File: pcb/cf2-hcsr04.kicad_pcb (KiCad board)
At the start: 2 copper layers, 25.2 x 27.3 mm, 3 parts, among them P1 CF_EXP_LEFT, P2 CF_EXP_RIGHT

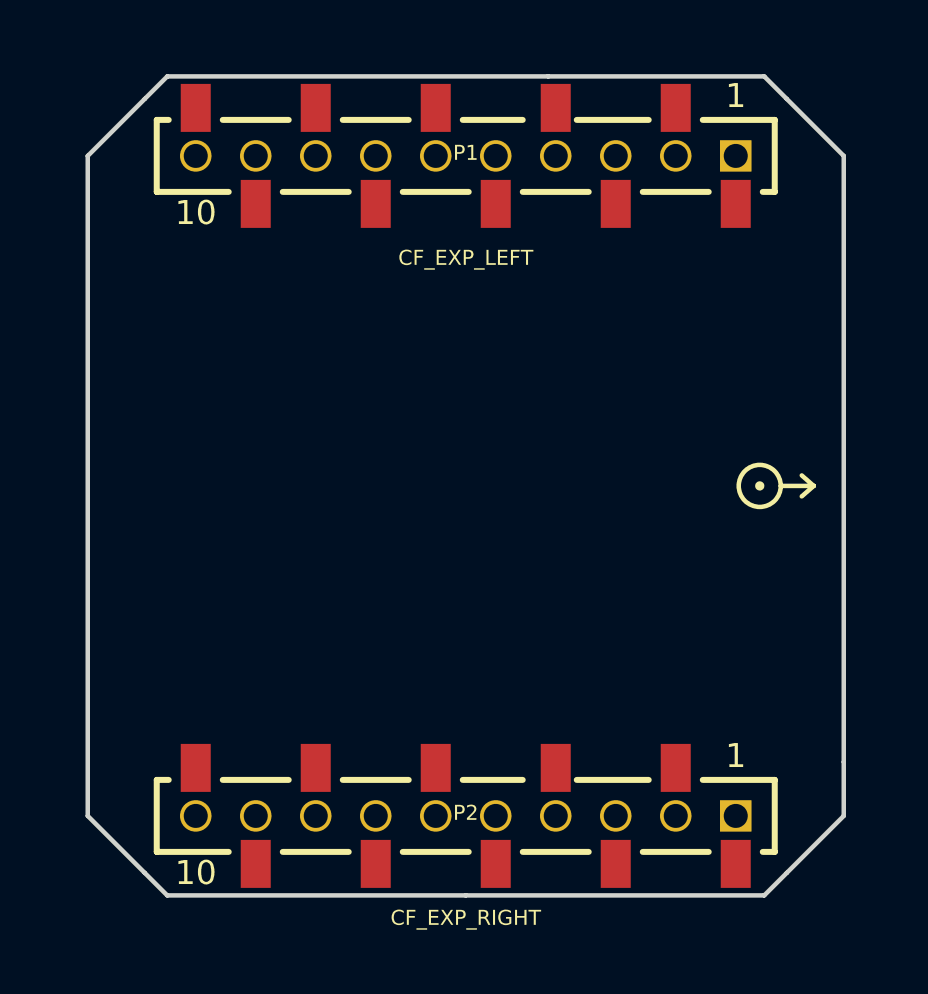
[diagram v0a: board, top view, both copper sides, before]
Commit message: Started work on footprint
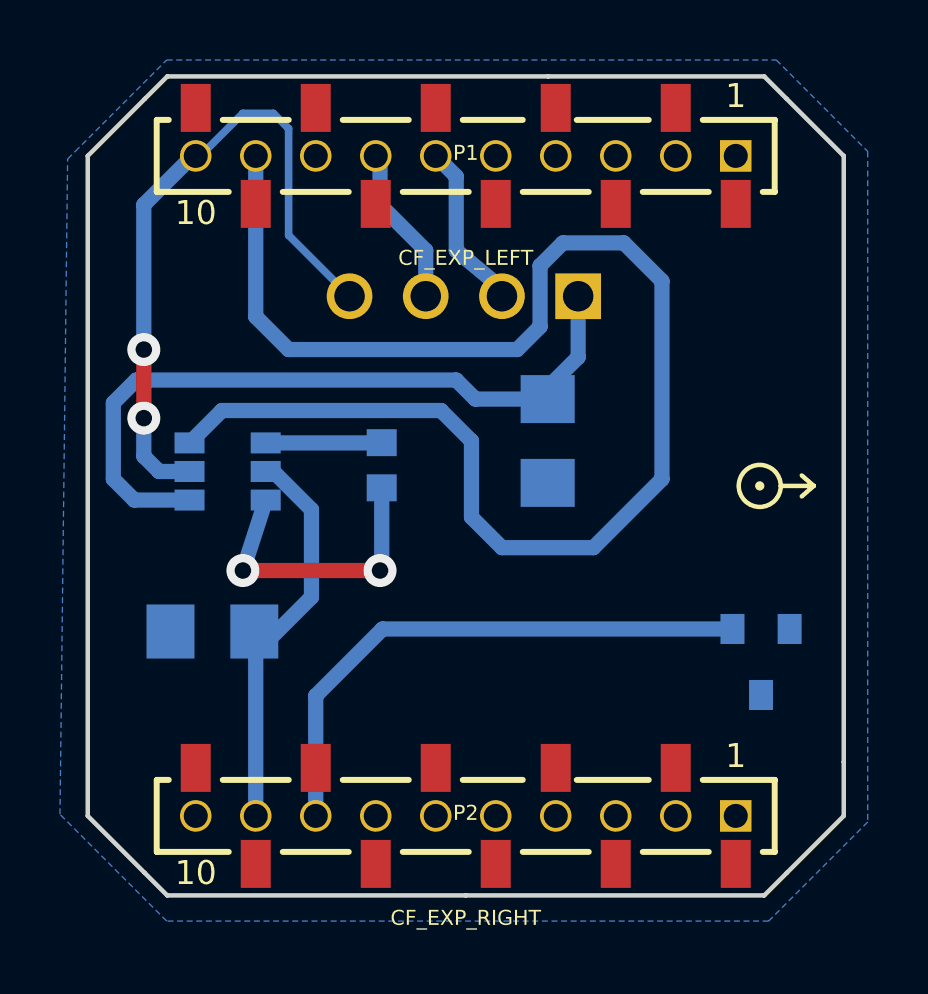
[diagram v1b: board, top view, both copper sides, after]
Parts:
- removed the EXP_ORIENTATION at (148.8, 97.0)
- added C1: 2.2uF, c_1206, B.Cu at (141.7, 95.5)
- added C2: 2.2uF, c_1206, B.Cu at (130.6, 101.9)
- added C3: 0.22uF, c_0603, B.Cu at (136.2, 96.3)
- added EXP_ORIENTATION: VAL**, bitcraze:EXP_ORIENTATION_B_MASK, F.Cu at (148.8, 97.0)
- added U1: DS28E05, SOT23, B.Cu at (148.8, 102.9)
- added U2: REG71050, SOT23_6, B.Cu at (131.1, 96.5)
- added U3: HC-SR04, PIN_ARRAY_4x1, B.Cu at (138.9, 90.7)
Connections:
- P1 pad 1: Net-(P1-Pad1) -> (no net)
- P1 pad 10: Net-(P1-Pad10) -> GND
- P1 pad 2: Net-(P1-Pad2) -> (no net)
- P1 pad 3: Net-(P1-Pad3) -> (no net)
- P1 pad 4: Net-(P1-Pad4) -> (no net)
- P1 pad 5: Net-(P1-Pad5) -> (no net)
- P1 pad 6: Net-(P1-Pad6) -> /IO_1
- P1 pad 7: Net-(P1-Pad7) -> /IO_2
- P1 pad 8: Net-(P1-Pad8) -> (no net)
- P1 pad 9: Net-(P1-Pad9) -> /IO_4
- P2 pad 1: Net-(P2-Pad1) -> (no net)
- P2 pad 10: Net-(P2-Pad10) -> (no net)
- P2 pad 2: Net-(P2-Pad2) -> (no net)
- P2 pad 3: Net-(P2-Pad3) -> (no net)
- P2 pad 4: Net-(P2-Pad4) -> (no net)
- P2 pad 5: Net-(P2-Pad5) -> (no net)
- P2 pad 6: Net-(P2-Pad6) -> (no net)
- P2 pad 7: Net-(P2-Pad7) -> (no net)
- P2 pad 8: Net-(P2-Pad8) -> /OW
- P2 pad 9: Net-(P2-Pad9) -> /VCOM
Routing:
- net /IO_4: track 0.00 -> 49.7 mm
- net N-0000022: track 0.00 -> 24.3 mm
- net GND: track 0.00 -> 22.8 mm, vias 0 -> 2
- net /OW: track 0.00 -> 18.8 mm
- net /VCOM: track 0.00 -> 13.8 mm
- net N-0000021: track 0.00 -> 9.82 mm, vias 0 -> 2
- net /IO_1: track 0.00 -> 5.67 mm
- net /IO_2: track 0.00 -> 5.37 mm
- net N-0000023: track 0.00 -> 3.87 mm
- added copper zone on B.Cu, net GND
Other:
- net class Default: via_dia 0.635 -> 1.1; via_drill 0.381 -> 1
